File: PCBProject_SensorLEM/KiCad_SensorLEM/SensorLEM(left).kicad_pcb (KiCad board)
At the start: 4 copper layers, 111.6 x 25.6 mm, 79 parts, among them J1 HIF3FC-30PA-2.54DSA, U1 ADR423ARZ

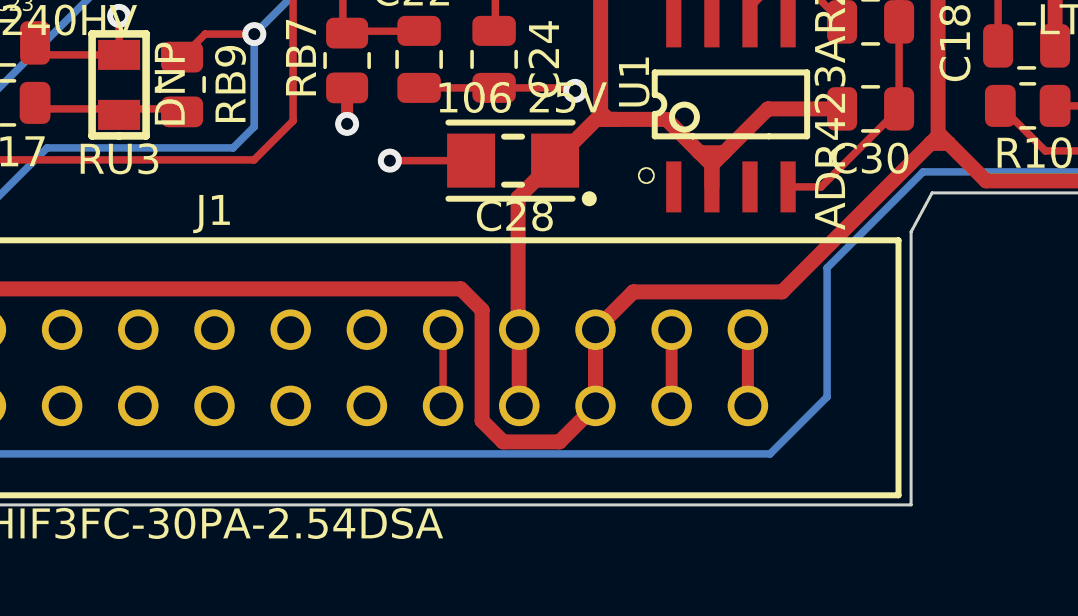
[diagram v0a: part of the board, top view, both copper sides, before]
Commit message: 完善电流传感器Pcb(只是加了30pin丝印)
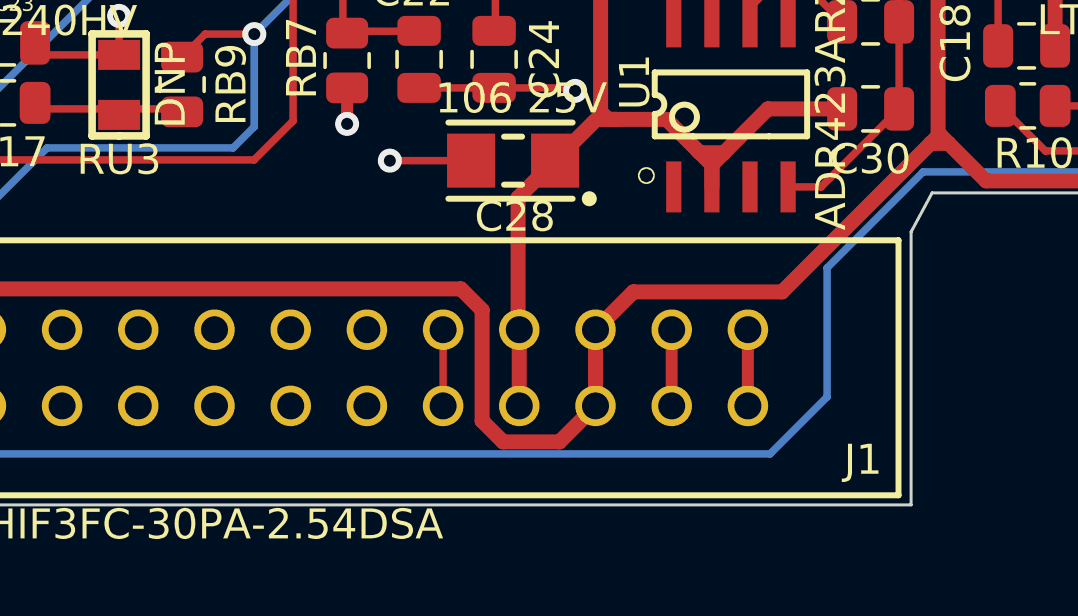
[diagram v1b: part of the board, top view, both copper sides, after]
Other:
- board text added: "SensorLEM(left)"
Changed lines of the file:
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@@
     (property "Sheetname" "")
     (property "ki_description" "Connector")
-    (fp_text reference "J1" (at 17.78 -6.495) (layer "F.SilkS")
+    (fp_text reference "J1" (at 39.4 1.8 180) (layer "F.SilkS")
         (effects (font (size 1 1) (thickness 0.15)))
     )
@@
     (property "Sheetname" "")
     (property "ki_description" "Current Sensor 50A 1 Channel Hall Effect, Closed Loop Bidirectional Module, Single Pass Through")
-    (fp_text reference "A5" (at -17.13 6.275) (layer "B.SilkS")
+    (fp_text reference "A5" (at -17.03 5.675 180) (layer "B.SilkS")
         (effects (font (size 1 1) (thickness 0.15)) (justify mirror))
     )
@@
     (property "Sheetname" "")
     (property "ki_description" "Current Sensor 50A 1 Channel Hall Effect, Closed Loop Bidirectional Module, Single Pass Through")
-    (fp_text reference "A4" (at -17 6.2) (layer "B.SilkS")
+    (fp_text reference "A4" (at -17 6.2 180) (layer "B.SilkS")
         (effects (font (size 1 1) (thickness 0.15)) (justify mirror))
     )
@@
   (gr_line (start 215.5 93.4) (end 215.5 108.6)
     (stroke (width 0.1) (type default)) (layer "Edge.Cuts"))
+  (gr_text "SensorLEM(left)" (at 105.9 108.8 90) (layer "B.SilkS")
+    (effects (font (size 0.8 0.8) (thickness 0.1)) (justify left bottom mirror))
+  )
   (segment (start 160.7 94.1) (end 160.6 94.1) (width 0.5) (layer "F.Cu") (net 1))
   (segment (start 160.4 94.1) (end 160.4 94.5) (width 0.5) (layer "F.Cu") (net 1))

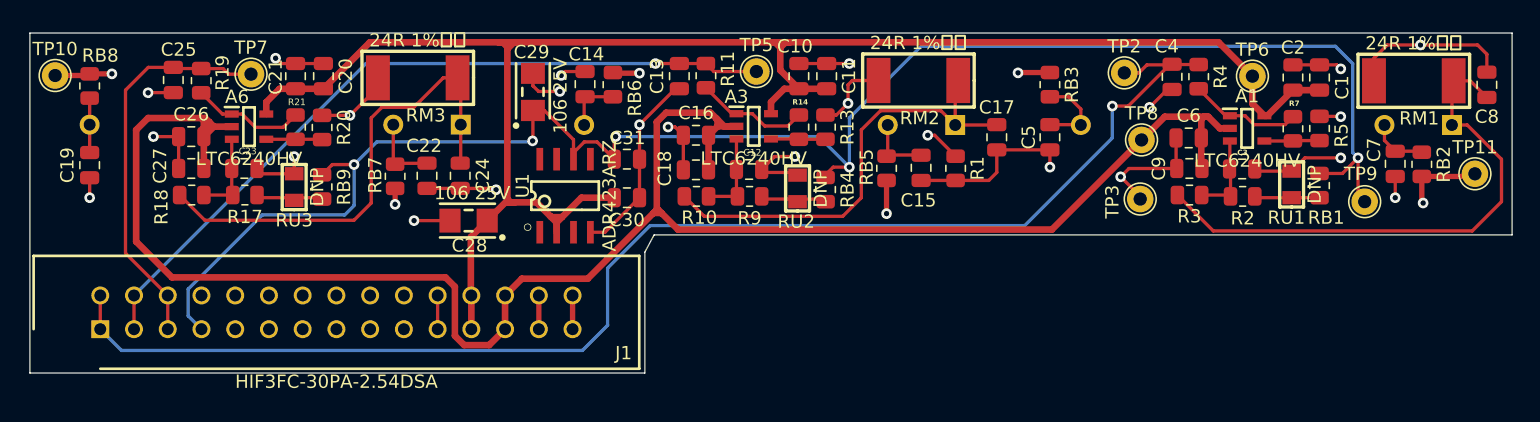
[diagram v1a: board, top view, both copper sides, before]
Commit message: 解决电流传感器中的错误：电线与边缘太近了！
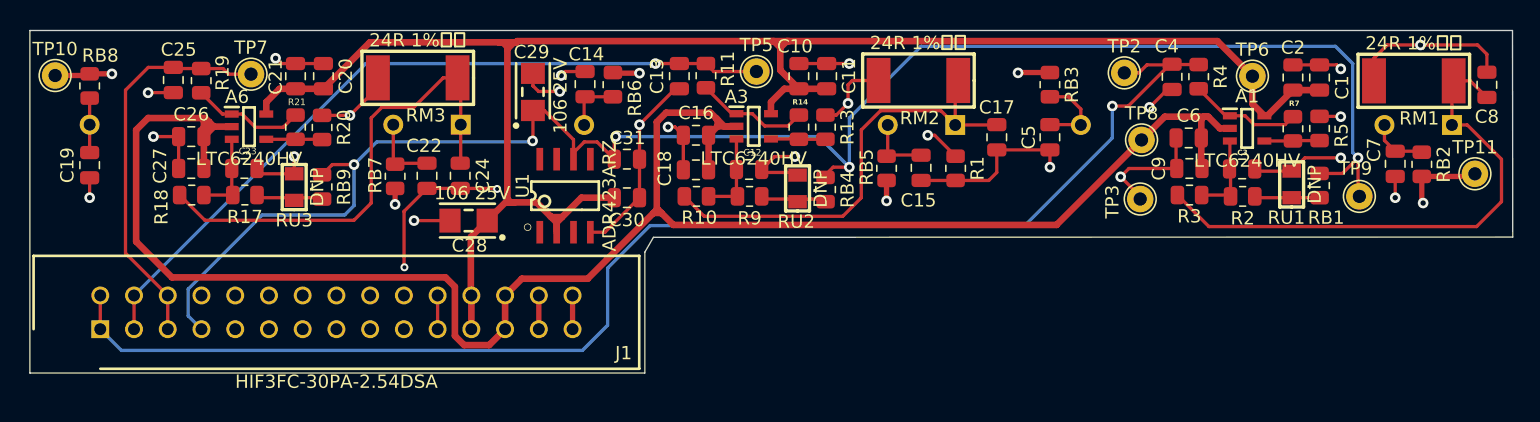
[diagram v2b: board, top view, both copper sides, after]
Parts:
- moved TP9 0.57 mm to (204.0, 105.7)
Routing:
- net 12VGND: track 51.0 -> 59.9 mm, vias 9 -> 10
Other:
- board size 111.6 x 25.6 mm -> 111.7 x 25.8 mm
